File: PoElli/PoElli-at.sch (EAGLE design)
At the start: 76 parts, among them J1 DF12-60DP, T1 POE-ISOLATION, U3 NCP1117, X1 RJ45MOLEX

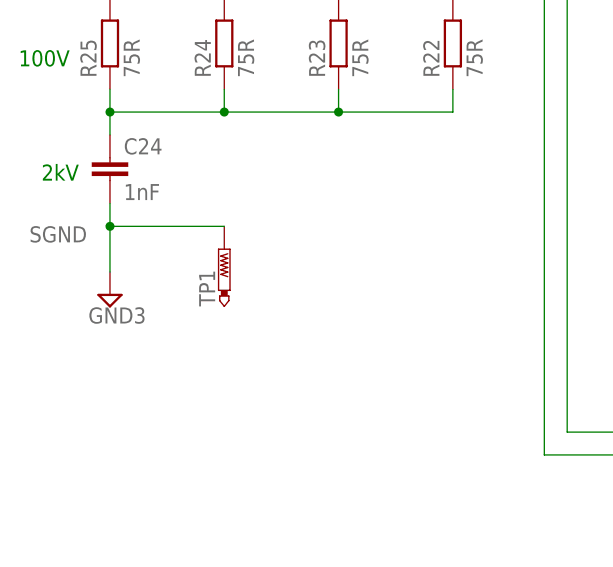
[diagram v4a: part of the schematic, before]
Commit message: Changed test point library
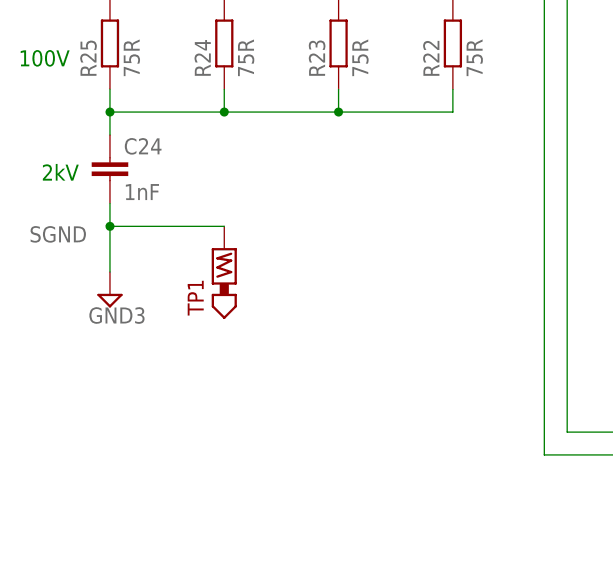
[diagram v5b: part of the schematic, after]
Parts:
- TP1: value PTR1B2,54 -> TEST_POINT-BARE; device testpad:PTR1B2,54 -> ELL-i-Passives:TEST_POINT-BARE
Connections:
- net SGND: now also TP1.P$1; no longer TP1.TP
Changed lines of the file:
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@@
 <part name="C23" library="ELL-i-Passives" deviceset="C" device="0805" value="10nF"/>
 <part name="C24" library="ELL-i-Passives" deviceset="C" device="0805" value="1nF"/>
-<part name="TP1" library="testpad" deviceset="PTR1" device="B2,54"/>
 <part name="SUPPLY1" library="supply2" deviceset="GND3" device=""/>
+<part name="TP1" library="ELL-i-Passives" deviceset="TEST_POINT" device="-BARE"/>
 </parts>
 <sheets>
@@
 <instance part="C23" gate="G$1" x="-124.46" y="121.92"/>
 <instance part="C24" gate="G$1" x="-124.46" y="93.98"/>
-<instance part="TP1" gate="G$1" x="-111.76" y="83.82"/>
 <instance part="SUPPLY1" gate="G$1" x="-124.46" y="78.74"/>
+<instance part="TP1" gate="TP$1" x="-111.76" y="83.82"/>
 </instances>
 <busses>
@@
 <pinref part="C24" gate="G$1" pin="2"/>
 <wire x1="-124.46" y1="81.28" x2="-124.46" y2="86.36" width="0.1524" layer="91"/>
-<pinref part="TP1" gate="G$1" pin="TP"/>
 <wire x1="-124.46" y1="86.36" x2="-124.46" y2="88.9" width="0.1524" layer="91"/>
 <wire x1="-111.76" y1="86.36" x2="-124.46" y2="86.36" width="0.1524" layer="91"/>
 <junction x="-124.46" y="86.36"/>
 <label x="-127" y="86.36" size="1.778" layer="95" rot="R180"/>
-</segment>
-</net>
+<pinref part="TP1" gate="TP$1" pin="P$1"/>
+</segment>
+</net>

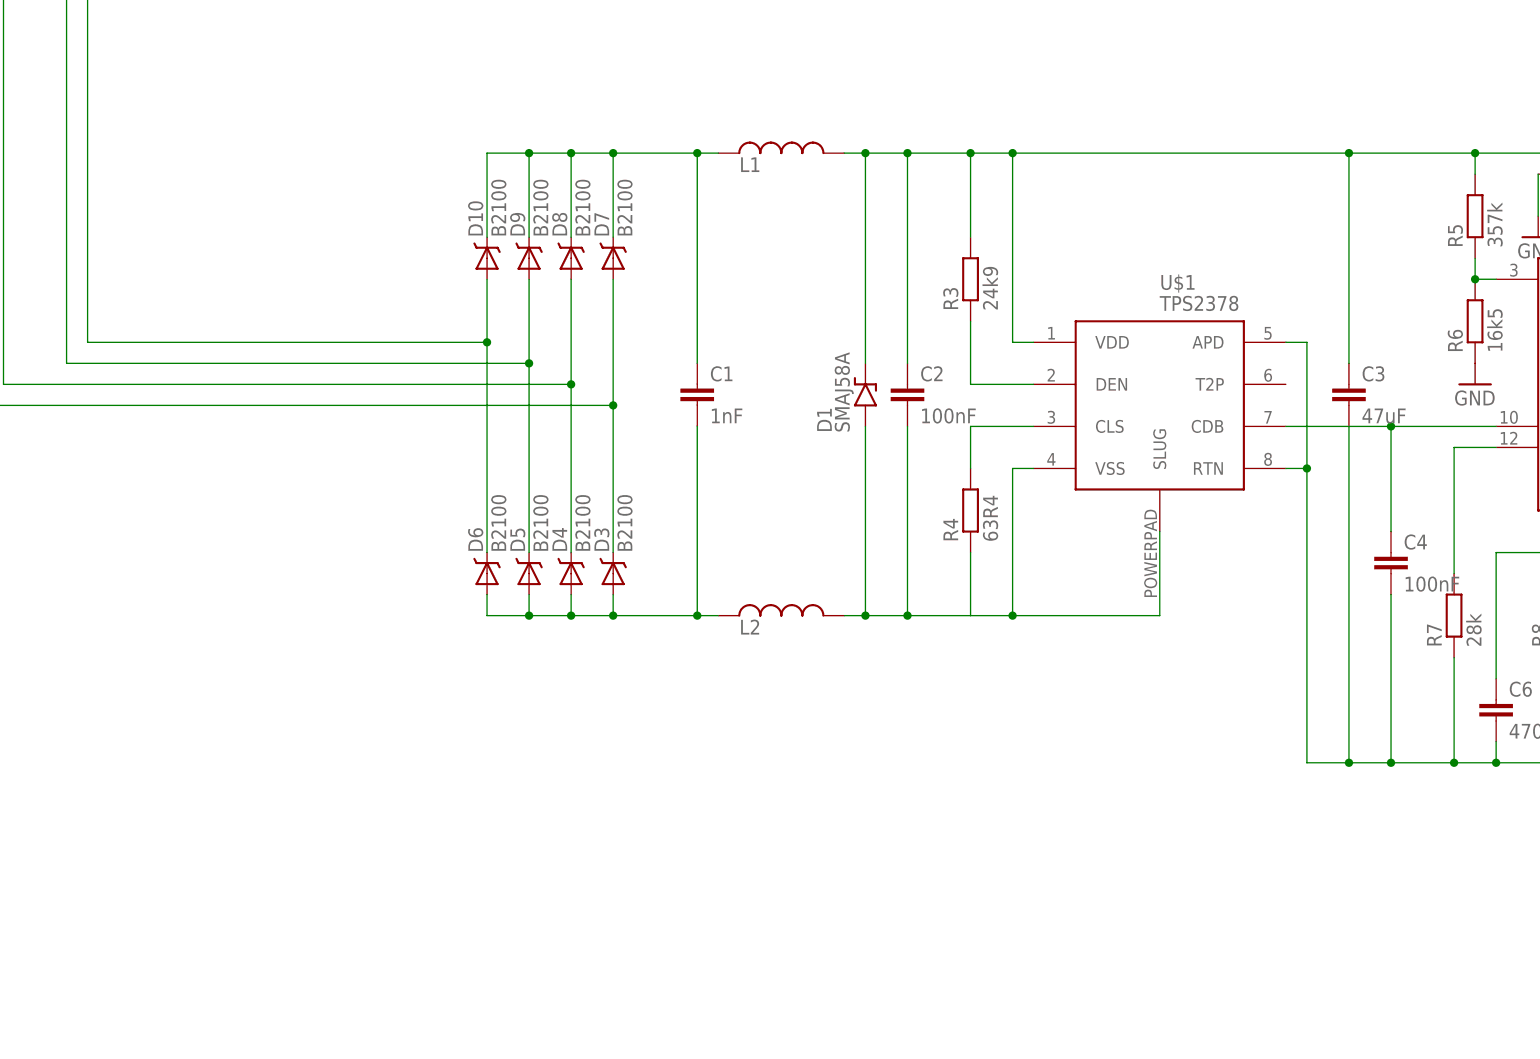
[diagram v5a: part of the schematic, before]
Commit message: Added external power connection
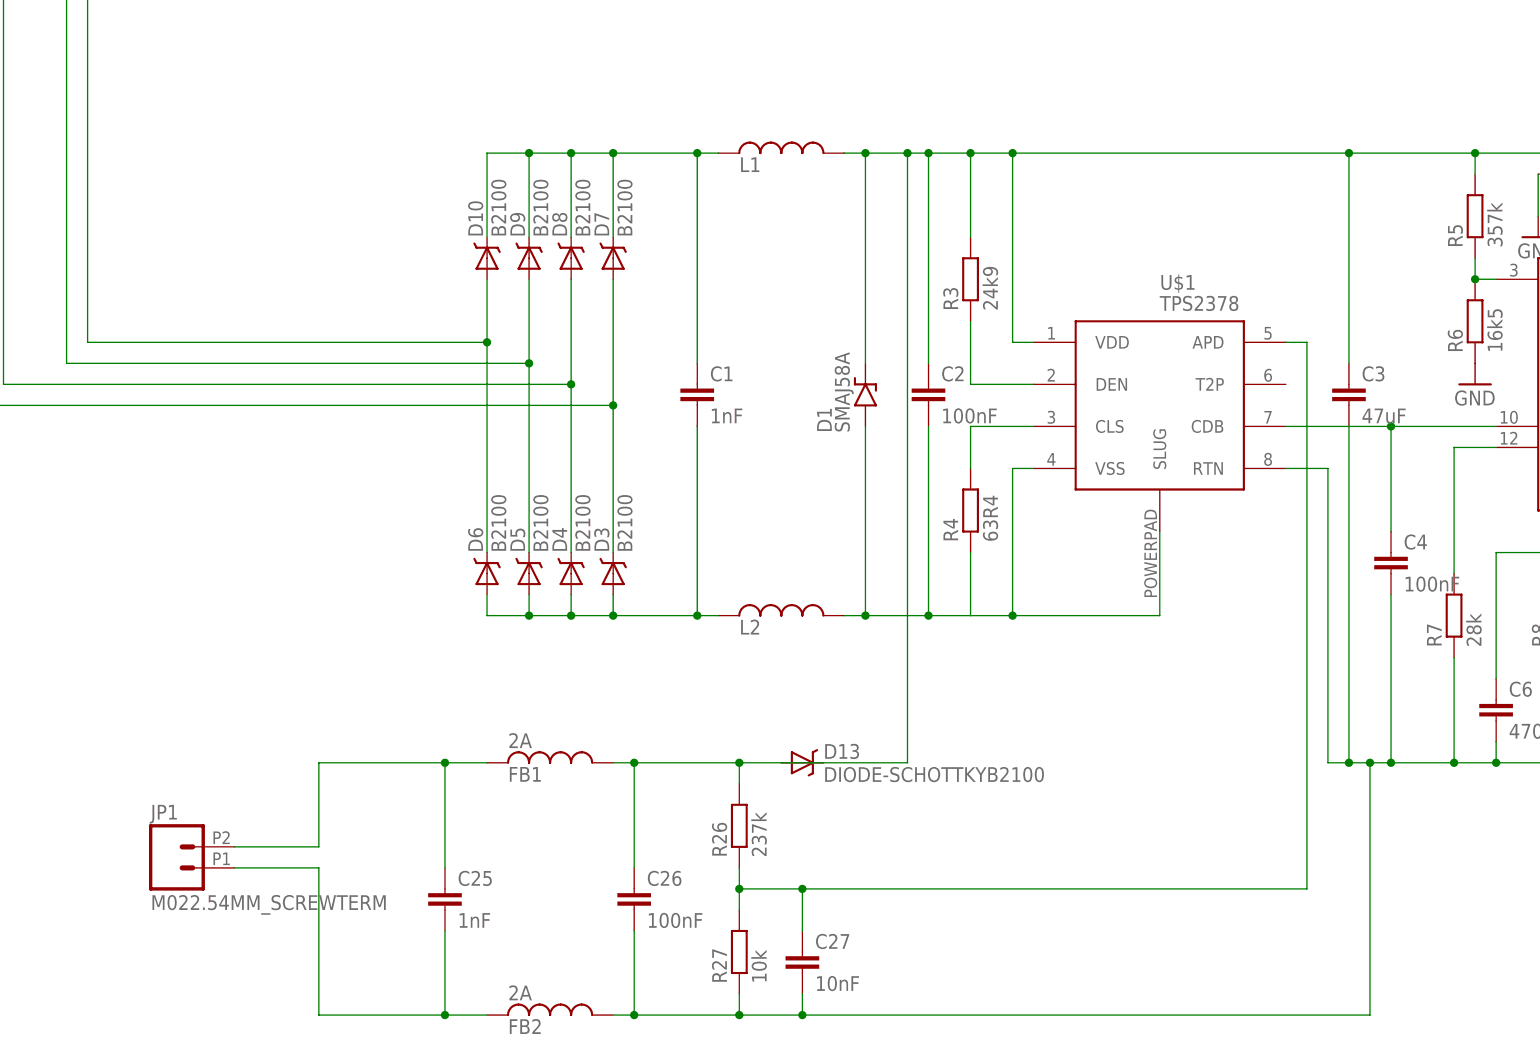
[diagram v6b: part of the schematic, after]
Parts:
- added C25: 1nF, ELL-i-Passives:C0805
- added C26: 100nF, ELL-i-Passives:C0805
- added C27: 10nF, ELL-i-Passives:C0805
- added D13: DIODE-SCHOTTKYB2100, ELL-i-DIscreteSemi:DIODE-SCHOTTKYB2100
- added FB1, FB2: 2A, ELL-i-Passives:FB
- added JP1: M022.54MM_SCREWTERM, SparkFun-Connectors:M022.54MM_SCREWTERM
- added R26: 237k, ELL-i-Passives:R0805
- added R27: 10k, ELL-i-Passives:R0805
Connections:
- new net N$53: C25.1, FB1.1, JP1.2
- new net N$54: C27.1, R26.1, R27.2, U$1.APD
- new net N$55: C25.2, FB2.1, JP1.1
- net GND: now also C26.2, C27.2, FB2.2, R27.1; no longer U$1.APD
- net N$16: now also C26.1, D13.A, D13.C, FB1.2, R26.2
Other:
- moved on the sheet: C2

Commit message: Add mux
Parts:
- added JP2: (no value), SparkFun-Connectors:M04LOCK
- added Q1: FDV301N, ELL-i-DIscreteSemi:FDV301N
- added Q2: SI1307DL, ELL-i-DIscreteSemi:SI1307DL
- added R$, R28: 100k, ELL-i-Passives:R0805
- added U1: FST3257, ELL-i-DigitalIC:FST3257
- C11: value 10n -> (none); device ELL-i-Passives:C0603 -> ELL-i-Passives:C0805
- C12: value 6.8n -> (none); device ELL-i-Passives:C0603 -> ELL-i-Passives:C0805
- C13: value 6.8n -> 100nF; device ELL-i-Passives:C0603 -> ELL-i-Passives:C0805
- C14: value 10n -> 100nF; device ELL-i-Passives:C0603 -> ELL-i-Passives:C0805
- R1: value 49.9,1% -> (none); device ELL-i-Passives:R0603 -> ELL-i-Passives:R0805
- R18, R2: value 49.9,1% -> 0R; device ELL-i-Passives:R0603 -> ELL-i-Passives:R0805
- R19: value 10R, 1% -> (none); device ELL-i-Passives:R0603 -> ELL-i-Passives:R0805
- R20: value 49.9,1% -> 1k; device ELL-i-Passives:R0603 -> ELL-i-Passives:R0805
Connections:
- removed net +3V3: C16.+, R18.1, R19.2, R2.2, U$4.VDD, U$4.VDDOSC, U$4.VDDPLL, U$4.VDDRX, U$4.VDDTX, U$4.VDD_2, U$4.VDD_3, U3.OUT, U3.TAB
- new net +5V0: C16.+, R1.2, R18.2, R2.2, U$4.VDD, U$4.VDDOSC, U$4.VDDPLL, U$4.VDDRX, U$4.VDDTX, U$4.VDD_2, U$4.VDD_3, U3.OUT, U3.TAB
- new net 3.3V: C11.1, C12.1, C14.2, Q1.S, R19.1
- new net MUX_ETH: Q1.G, R$.2, R19.2, U1.S
- new net N$56: Q1.D, R20.1
- new net N$57: Q2.G, R20.2, R28.1
- new net N$58: C14.1, Q2.S, R28.2
- new net N$60: Q2.D
- new net RX+: JP2.2, U1.2B0
- new net RX-: JP2.1, U1.1A0
- new net TX+: JP2.4, U1.4D0
- new net TX-: JP2.3, U1.3C0
- net GNDA: no longer C11.2, C14.2
- net N$11: now also T1.TD+, U1.4D; no longer C14.1, R1.2, R20.1, T1.RCT
- net N$12: now also T1.TD-, U1.3C; no longer C13.1, T1.RD-
- net N$13: now also T1.RD+, U1.2B; no longer R18.2, T1.TD-, U$4.TPOUT+
- net N$14: now also T1.RD-, U1.1A; no longer R2.1, T1.TD+, U$4.TPOUT-
- net N$39: now also R$.1, U1.!EN, U1.GND; no longer C12.1, T1.RD+
- net N$40: now also C11.2, T1.TCT; no longer U$4.TPIN-
- net N$43: now also C13.1, R18.1, R2.1, U1.VCC; no longer C11.1, R19.1, T1.TCT
- net N$44: no longer R20.2, U$4.TPIN+
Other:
- moved on the sheet: C11, C12, C13, C14, C15, C18, C19, D11, D12, R1, R16, R17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

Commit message: Add placeholder components
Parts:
- removed R15: 100, ELL-i-Passives:R0805
- removed U$6: 10MQ100N, TPS2378:10MQ100N
- added C28, C29: 6n8, ELL-i-Passives:C0805
- added C30, C37, C39: 100nF, ELL-i-Passives:C0805
- added C31: 47pF, ELL-i-Passives:C0805
- added C32, C33, C34, C35, C36: 1nF, ELL-i-Passives:C0805
- added C38: 470pF, ELL-i-Passives:C0805
- added D14: BA340A, SparkFun-DiscreteSemi:B340A
- added FB3: LQM15, ELL-i-Passives:FB
- added R29, R30, R31, R32: 49R9, ELL-i-Passives:R0805
- added R33: 100k, ELL-i-Passives:R0805
- added R34: 10R, ELL-i-Passives:R0805
- added TP10, TP5, TP6, TP7, TP8, TP9: TEST_POINT-5000, ELL-i-Passives:TEST_POINT-5000
- added TP2, TP3, TP4: TEST_POINT-5021, ELL-i-Passives:TEST_POINT-5021
- added Y1: 25MHz, SparkFun-FreqCtrl:CRYSTAL5X3
- C10: value 47uF -> (none); device ELL-i-Passives:CPOL6032 -> ELL-i-Passives:CPOLC
- C17: value 100n -> 47pF
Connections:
- removed net 3.3V: C11.1, C12.1, C14.2, Q1.S, R19.1
- new net +3V3: C14.1, Q2.S, R1.2, R2.2, R28.2
- new net MISO_ETH: U$4.SO/WR/WRL/EN/BOSEL
- new net MOSI_ETH: U$4.SI/RD/R~W
- new net N$59: C29.2, R29.2, U$4.TPIN+
- new net N$61: C28.1, U1.1A1
- new net N$62: R31.1, U$4.TPOUT+, U1.4D1
- new net N$63: R32.1, U$4.TPOUT-, U1.3C1
- new net N$64: C29.1, U1.2B1
- new net N$65: TP5.P$1
- new net N$66: C38.1, R34.1
- new net N$67: TP6.P$1
- new net N$68: TP7.P$1
- new net N$69: TP8.P$1
- new net N$70: TP9.P$1
- new net N$71: TP10.P$1
- new net NINT_ETH: R33.1, U$4.~INT/SPISEL
- new net NSS_ETH: U$4.~CS/CS
- new net SCK_ETH: U$4.SCK/AL/PSPCFG4
- net +5V0: now also C31.2, C32.2, C33.2, C34.2, C35.1, C36.1, FB3.2, R31.2, R32.2, R33.2, TP2.P$1; no longer R1.2, R2.2
- net GNDA: now also C11.1, C12.1, C13.2, C14.2, C30.1, C31.1, C32.1, C33.1, C34.1, C35.2, C36.2, C37.2, Q1.S, R$.1, R19.1, U1.!EN, U1.GND; no longer C10.-, C16.-, C17.2, R15.1, U$7.SEC-, U3.GND
- net N$34: now also C38.2, D14.A; no longer U$6.A
- net N$35: now also C39.1, D14.C, R34.2, TP3.P$1; no longer R15.2, U$6.C
- net N$37: now also Y1.1
- net N$39: now also C28.2, R30.2, U$4.TPIN-; no longer R$.1, U1.!EN, U1.GND
- net N$44: now also C30.2, R29.1, R30.1; no longer C13.2
- net N$46: now also C37.1
- net N$47: now also Y1.2
- net N$58: now also C10.-, C16.-, C17.2, C39.2, TP4.P$1, U$7.SEC-, U3.GND; no longer C14.1, Q2.S, R28.2
- net N$60: now also FB3.1
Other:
- note added: "Add 5V1 zen"
- note added: "Add ground"
- note added: "WRONG FOOTPRINT FOR Y1"
- note removed: "6.3V"
- note removed: "Check: Original marking is R102K"
- moved on the sheet: C10, C16, C17, C18, C19, J1, U3
